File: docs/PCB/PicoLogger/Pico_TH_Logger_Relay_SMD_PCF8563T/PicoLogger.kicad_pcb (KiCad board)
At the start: 2 copper layers, 100.5 x 83 mm, 62 parts, among them J1 Sensor, J2 LCD 16x2, J3 Additional connector, J4 K4_Output, J5 K3_Output, J6 K2_Output, J7 K1_Output, K1 G5Q-1, K2 G5Q-1, K3 G5Q-1, K4 G5Q-1, Q1 MMBT3904, Q2 MMBT3904, Q3 MMBT3904, Q4 MMBT3904, SW1 SW_Push, SW2 SW_Push, U1 LTV-817S, U2 LTV-817S, U3 LTV-817S, U4 LTV-817S, U5 PCF8563T, Y1 Crystal

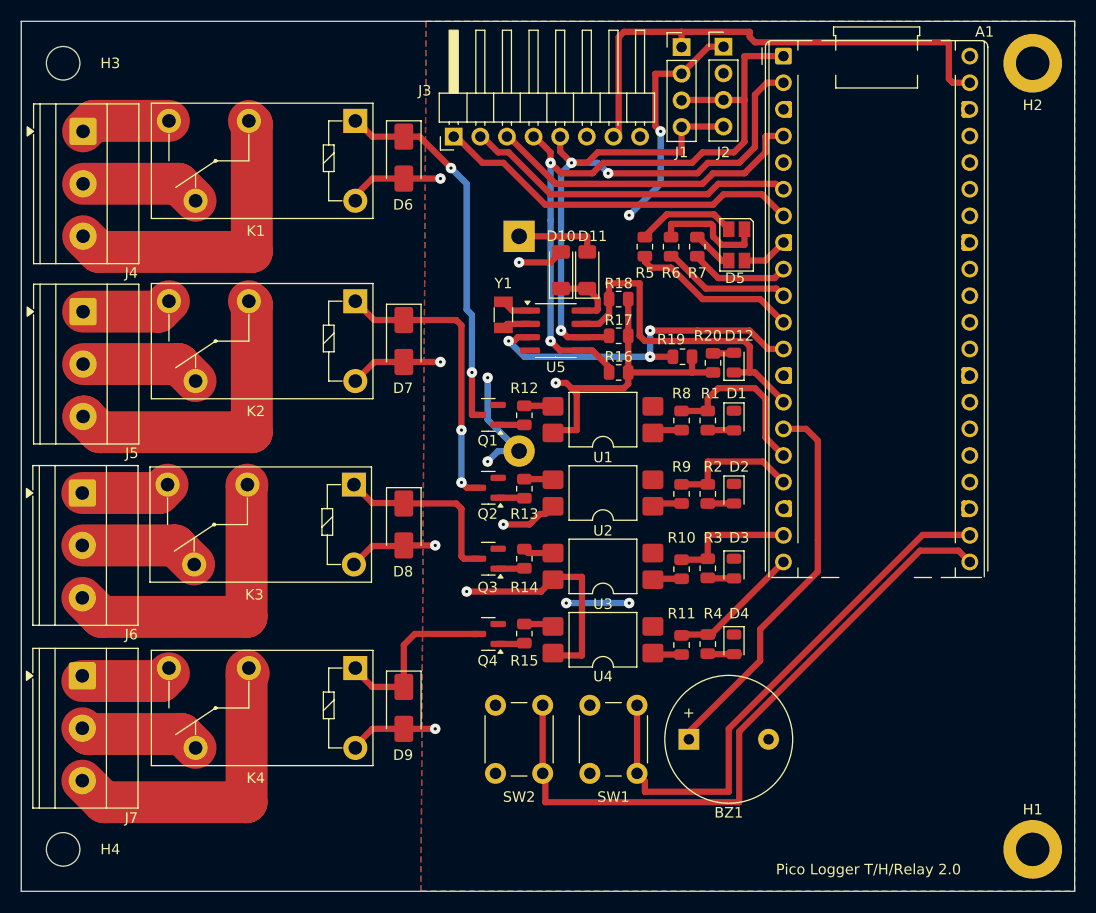
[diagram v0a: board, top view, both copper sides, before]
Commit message: Logger docs updated.
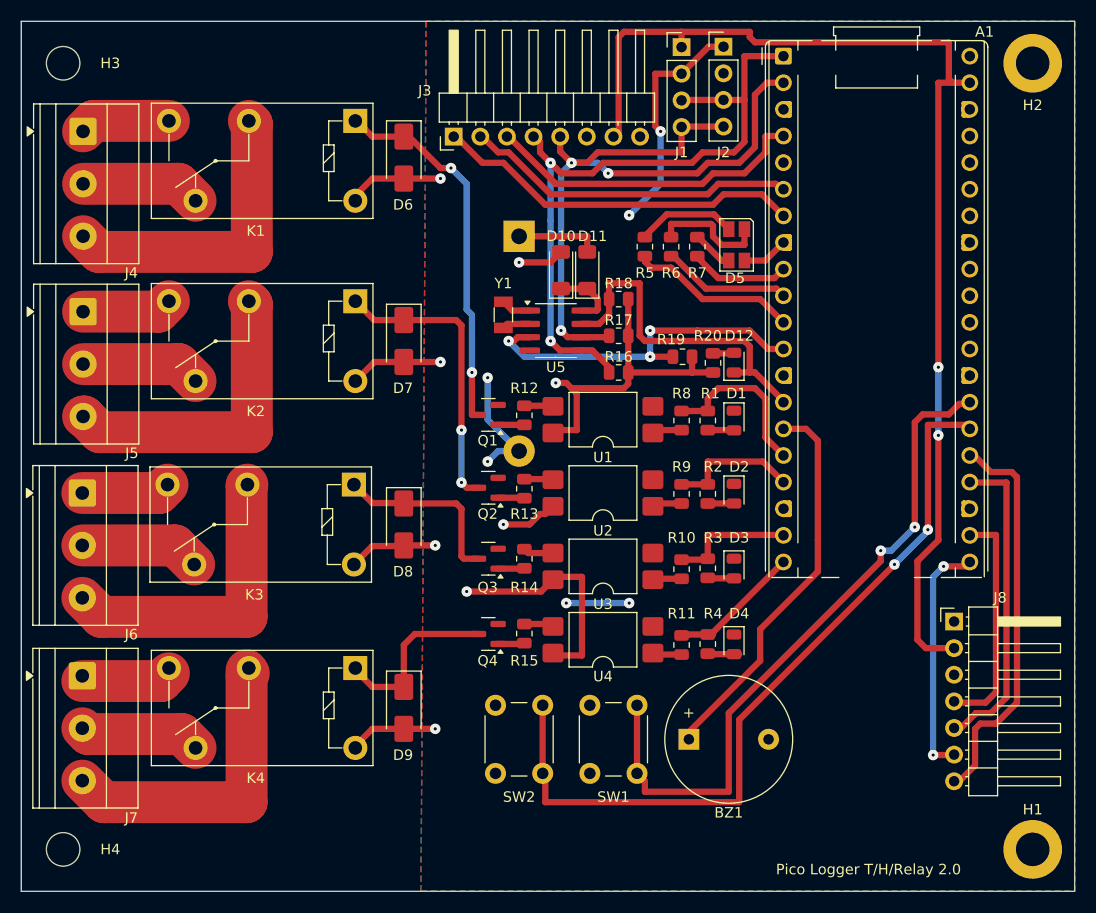
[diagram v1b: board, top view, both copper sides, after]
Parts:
- added J8: SPI, Connector_PinHeader_2.54mm:PinHeader_1x07_P2.54mm_Horizontal, F.Cu at (187.0, 103.3)
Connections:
- A1 pad 21: GPIO16 -> SPI RX
- A1 pad 22: GPIO17 -> SPI CSn
- A1 pad 24: unconnected-(A1-GPIO18-Pad24) -> SPI SCK
- A1 pad 25: unconnected-(A1-GPIO19-Pad25) -> SPI TX
- A1 pad 26: unconnected-(A1-GPIO20-Pad26) -> GPIO20
- A1 pad 27: unconnected-(A1-GPIO21-Pad27) -> GPIO21
- SW1 pad 2: GPIO17 -> GPIO21
- SW2 pad 2: GPIO16 -> GPIO20
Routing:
- net GPIO20: track 0.00 -> 75.6 mm, vias 0 -> 2
- net GPIO21: track 0.00 -> 65.8 mm, vias 0 -> 2
- net GPIO16: track 64.2 -> 0.00 mm
- net +3.3V: track 49.2 -> 108.4 mm, vias 0 -> 2
- net GPIO17: track 53.2 -> 0.00 mm
- net SPI TX: track 0.00 -> 38.0 mm
- net SPI SCK: track 0.00 -> 30.2 mm
- net SPI RX: track 0.00 -> 23.1 mm, vias 0 -> 2
- net SPI CSn: track 0.00 -> 22.0 mm

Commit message: Loggers corrected based on JLCPCB DFM check.
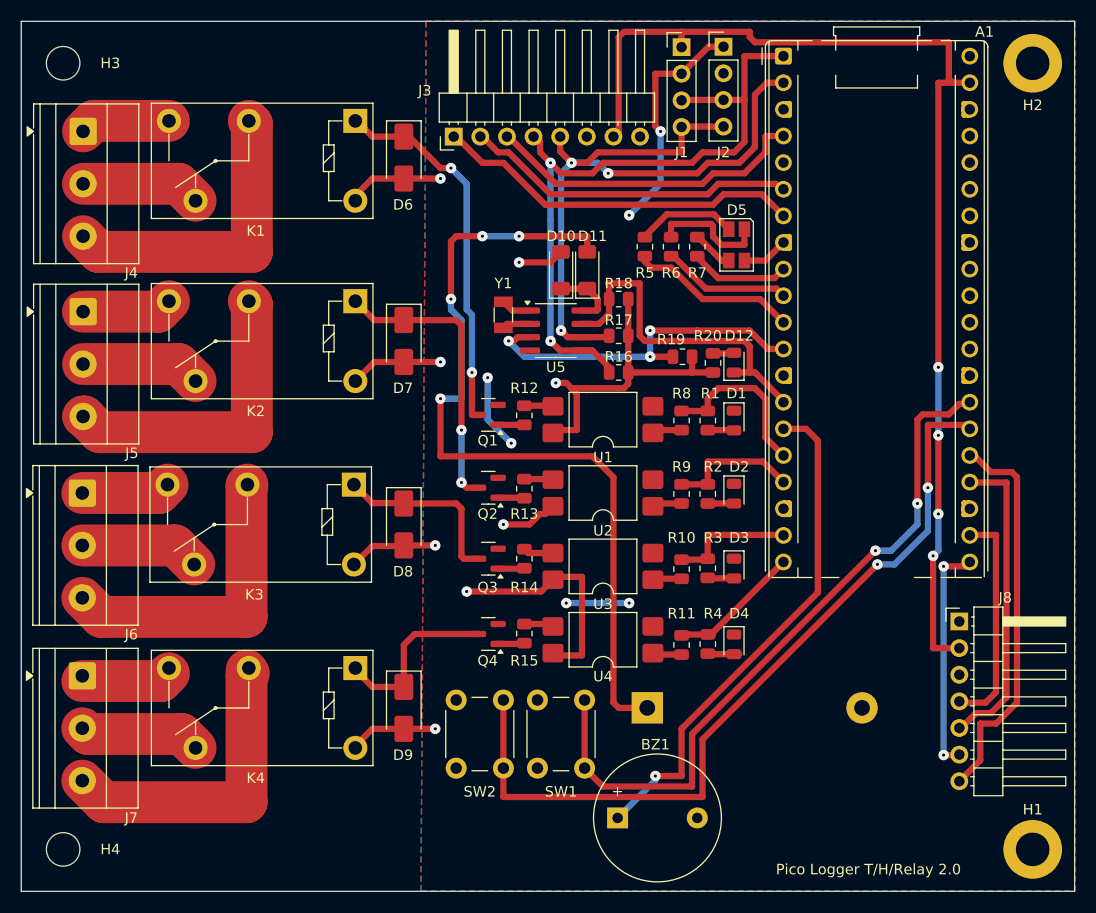
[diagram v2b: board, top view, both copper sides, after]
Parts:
- moved BT1 46.6 mm to (157.7, 111.5), turned to 0 degrees
- moved BZ1 10.1 mm to (154.9, 122.0)
- moved SW1 5.02 mm to (147.2, 117.2)
- moved SW2 3.78 mm to (139.5, 117.2)
- moved J8 0.50 mm to (187.5, 103.3)
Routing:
- net +BATT: track 8.00 -> 79.9 mm, vias 0 -> 4
- net GPIO11: track 36.6 -> 49.1 mm, vias 0 -> 1
- net GND: track 44.6 -> 40.1 mm
- net GPIO20: track 75.6 -> 77.8 mm
- net GPIO21: track 65.8 -> 67.9 mm
- net +3.3V: track 108.4 -> 106.7 mm, vias 2 -> 4
- net SPI RX: track 23.1 -> 21.7 mm

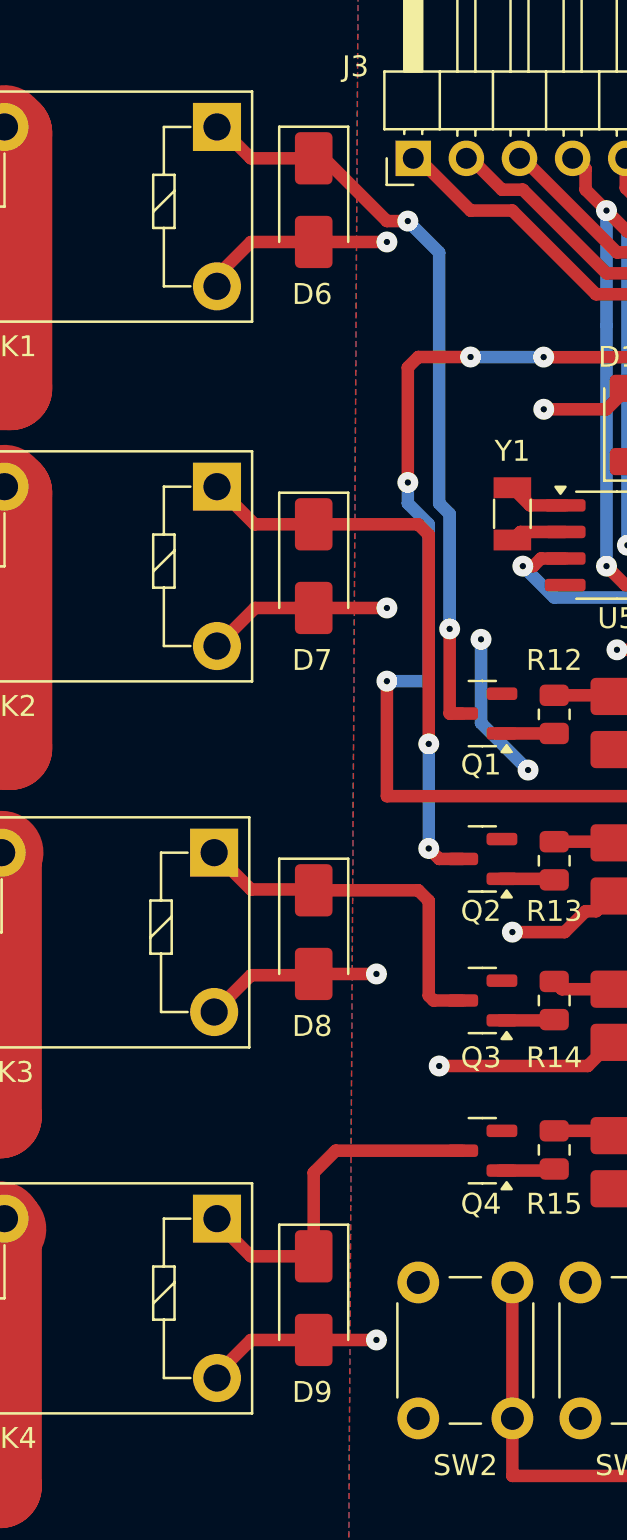
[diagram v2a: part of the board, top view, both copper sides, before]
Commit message: Pico1 and Pico2 devices code implemented.
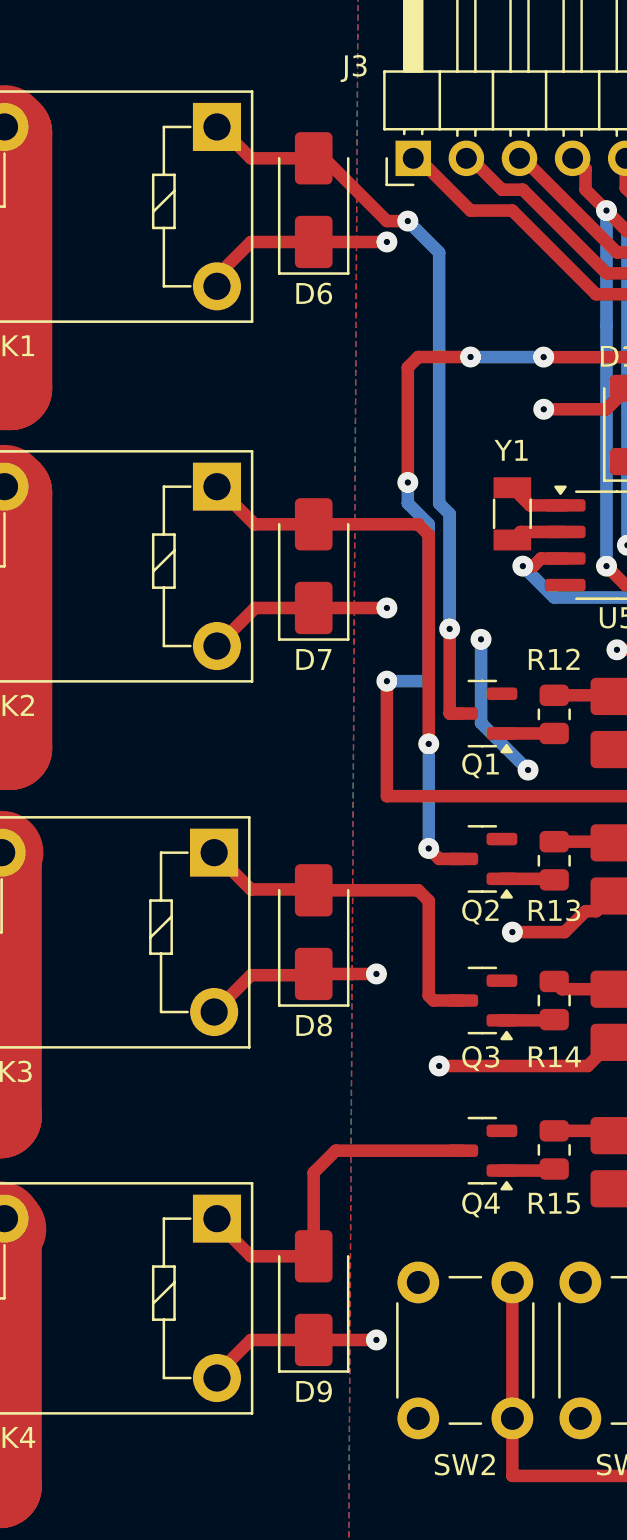
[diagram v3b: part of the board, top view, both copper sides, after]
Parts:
- turned D6 to 90 degrees
- turned D7 to 90 degrees
- turned D8 to 90 degrees
- turned D9 to 90 degrees
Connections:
- D6 pad 1: K1_Pin1 -> K1_Pin5
- D6 pad 2: K1_Pin5 -> K1_Pin1
- D7 pad 1: K2_Pin1 -> K1_Pin5
- D7 pad 2: K1_Pin5 -> K2_Pin1
- D8 pad 1: K3_Pin1 -> K1_Pin5
- D8 pad 2: K1_Pin5 -> K3_Pin1
- D9 pad 1: K4_Pin1 -> K1_Pin5
- D9 pad 2: K1_Pin5 -> K4_Pin1

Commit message: Updated docs.
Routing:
- net +3.3V: track 106.7 -> 104.4 mm
- net SDA: track 65.4 -> 63.5 mm
- net K4_Pin2: track 29.4 -> 27.7 mm
- net Net-(D10-K): track 6.48 -> 4.81 mm
- net K3_Pin2: track 29.1 -> 27.4 mm
- net SPI TX: track 38.0 -> 36.6 mm
- net K1_Pin5: track 97.8 -> 96.4 mm
- net K1_Pin2: track 29.3 -> 27.9 mm
- net GPIO20: track 77.8 -> 76.3 mm
- net K2_Pin2: track 29.3 -> 28.1 mm
- net GPIO21: track 67.9 -> 66.8 mm
- net GPIO2: track 31.2 -> 30.3 mm
- net GPIO10: track 33.2 -> 32.5 mm
- net +BATT: track 79.9 -> 79.3 mm
- net GPIO11: track 49.1 -> 48.5 mm
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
